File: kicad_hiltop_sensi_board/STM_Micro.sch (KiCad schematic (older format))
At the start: 19 parts, among them SW1 SW_Push, U22 STM32F072RBTx, Y2 8MHZ, Y3 ABS25-32.768KHZ-6-T

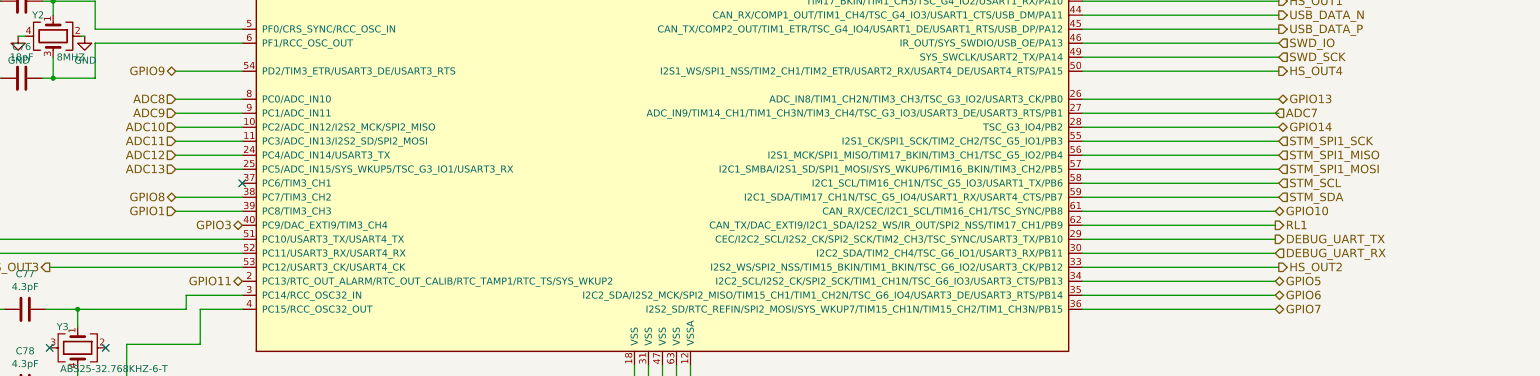
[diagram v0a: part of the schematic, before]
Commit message: Changes to Sensi board after review
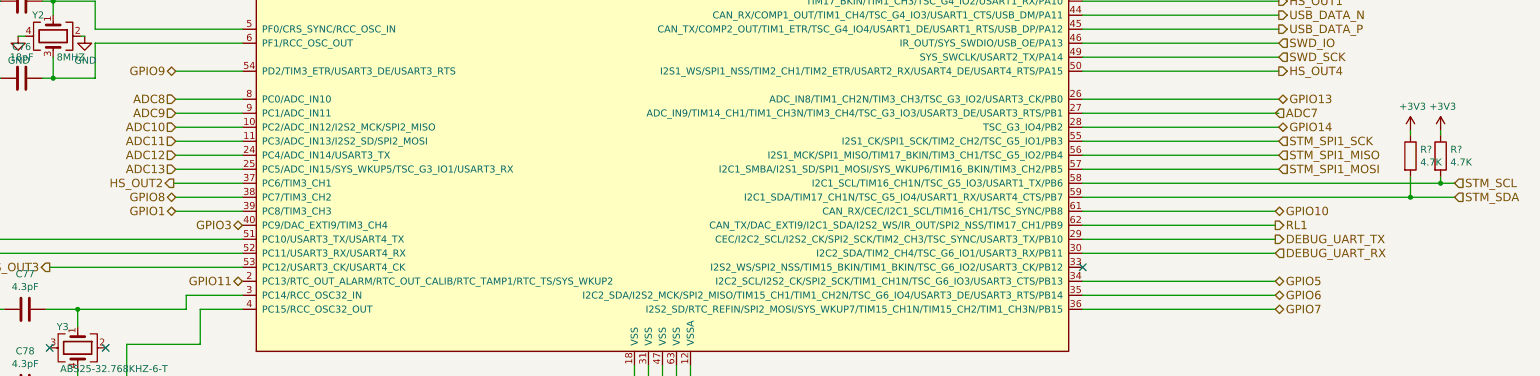
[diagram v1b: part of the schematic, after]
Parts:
- added R? (x2): 4.7K, symbol device:R
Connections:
- net +3V3: now also R?.1, R?.1
- net HS_OUT2: now also U22.37 (PC6/TIM3_CH1); no longer U22.33 (I2S2_WS/SPI2_NSS/TIM15_BKIN/TIM1_BKIN/TSC_G6_IO2/USART3_CK/PB12)
- net STM_SCL: now also R?.2
- net STM_SDA: now also R?.2
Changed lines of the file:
@@
 	10400 4575 11800 4575
 Wire Wire Line
-	10400 5475 11800 5475
+	10400 5475 12740 5475
 Wire Wire Line
 	10400 5575 11775 5575
@@
 	10400 4975 11800 4975
 Wire Wire Line
-	10400 5375 11800 5375
+	10400 5375 12955 5375
 Wire Wire Line
 	10400 6175 11775 6175
@@
 Text HLabel 2500 5775 0    60   BiDi ~ 0
 DUT1_UART_RX_GPIO15
-Text HLabel 3925 5575 0    60   Input ~ 0
+Text HLabel 3925 5575 0    60   3State ~ 0
 GPIO1
 Wire Wire Line
@@
 Text HLabel 11800 5275 2    60   Input ~ 0
 STM_SPI1_MOSI
-Text HLabel 11800 5375 2    60   Input ~ 0
+Text HLabel 13055 5375 2    60   Input ~ 0
 STM_SCL
-Text HLabel 11800 5475 2    60   Input ~ 0
+Text HLabel 13055 5475 2    60   Input ~ 0
 STM_SDA
-NoConn ~ 4400 5375
 NoConn ~ 4400 3475
 NoConn ~ 3425 6550
@@
 Text HLabel 11800 3075 2    60   Input ~ 0
 ADC1
-Text HLabel 11800 5975 2    60   Output ~ 0
+Text HLabel 3910 5375 0    60   Output ~ 0
 HS_OUT2
 Text HLabel 4400 5675 0    60   BiDi ~ 0
@@
 Wire Wire Line
 	4400 5875 2500 5875
-Wire Wire Line
-	10400 5975 11800 5975
 Text HLabel 3925 4975 0    60   Input ~ 0
 ADC10
@@
 Wire Wire Line
 	3250 4325 3275 4325
+Wire Wire Line
+	4400 5375 3910 5375
+NoConn ~ 10400 5975
+$Comp
+L device:R R?
+U 1 1 63797E89
+P 12955 5180
+F 0 "R?" H 13025 5226 50  0000 L CNN
+F 1 "4.7K" H 13025 5135 50  0000 L CNN
+F 2 "" V 12885 5180 50  0001 C CNN
+F 3 "" H 12955 5180 50  0001 C CNN
+	1    12955 5180
+	1    0    0    -1
+$EndComp
+$Comp
+L device:R R?
+U 1 1 63798365
+P 12740 5180
+F 0 "R?" H 12810 5226 50  0000 L CNN
+F 1 "4.7K" H 12810 5135 50  0000 L CNN
+F 2 "" V 12670 5180 50  0001 C CNN
+F 3 "" H 12740 5180 50  0001 C CNN
+	1    12740 5180
+	1    0    0    -1
+$EndComp
+$Comp
+L power:+3V3 #PWR?
+U 1 1 63798567
+P 12740 5000
+F 0 "#PWR?" H 12740 4850 50  0001 C CNN
+F 1 "+3V3" H 12755 5173 50  0000 C CNN
+F 2 "" H 12740 5000 50  0001 C CNN
+F 3 "" H 12740 5000 50  0001 C CNN
+	1    12740 5000
+	1    0    0    -1
+$EndComp
+$Comp
+L power:+3V3 #PWR?
+U 1 1 6379878A
+P 12955 5000
+F 0 "#PWR?" H 12955 4850 50  0001 C CNN
+F 1 "+3V3" H 12970 5173 50  0000 C CNN
+F 2 "" H 12955 5000 50  0001 C CNN
+F 3 "" H 12955 5000 50  0001 C CNN
+	1    12955 5000
+	1    0    0    -1
+$EndComp
+Wire Wire Line
+	12955 5330 12955 5375
+Connection ~ 12955 5375
+Wire Wire Line
+	12955 5375 13055 5375
+Wire Wire Line
+	12740 5330 12740 5475
+Connection ~ 12740 5475
+Wire Wire Line
+	12740 5475 13055 5475
+Wire Wire Line
+	12740 5030 12740 5000
+Wire Wire Line
+	12955 5030 12955 5000
 $EndSCHEMATC

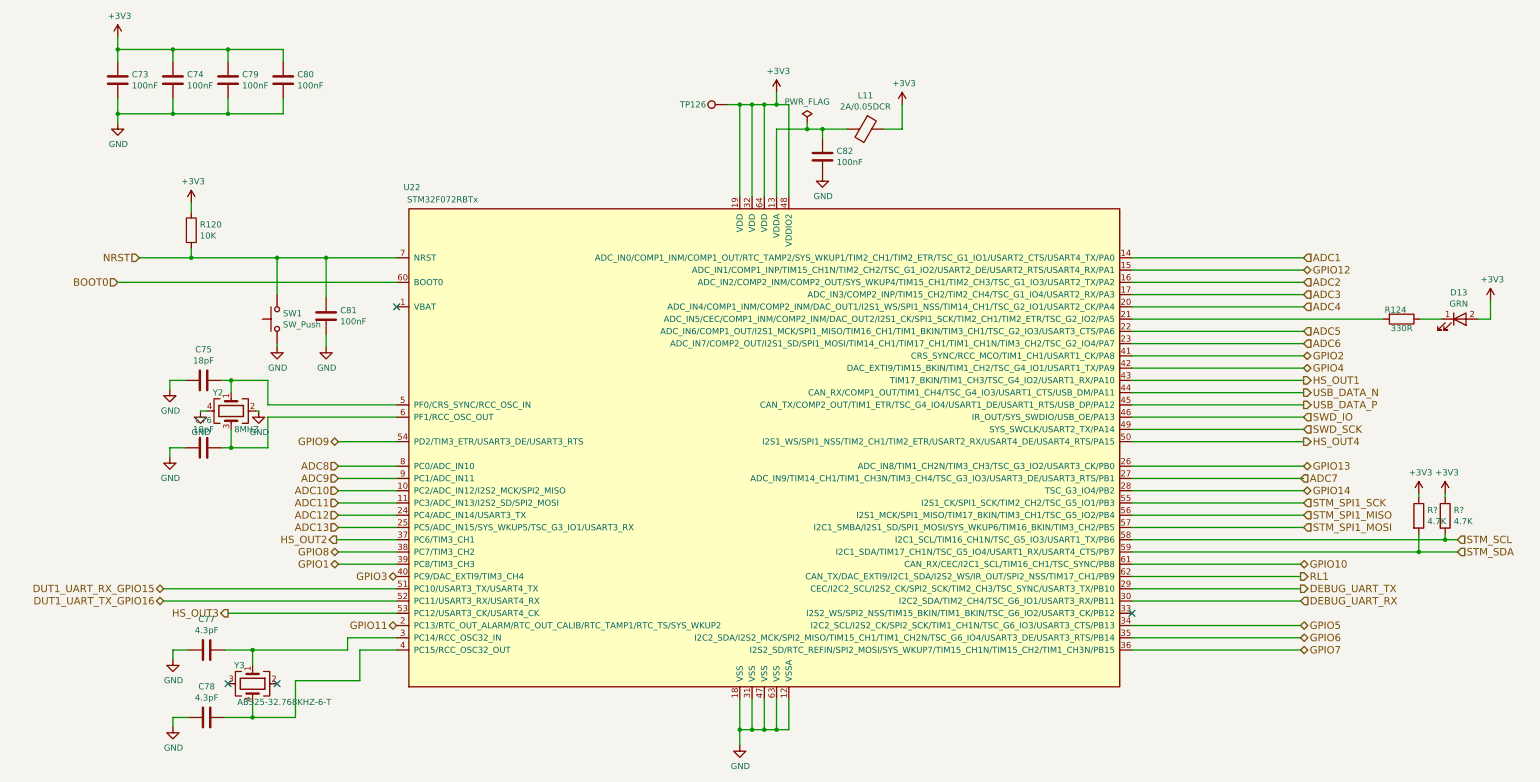
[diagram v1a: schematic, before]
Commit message: Sensi board schematic updated from comments
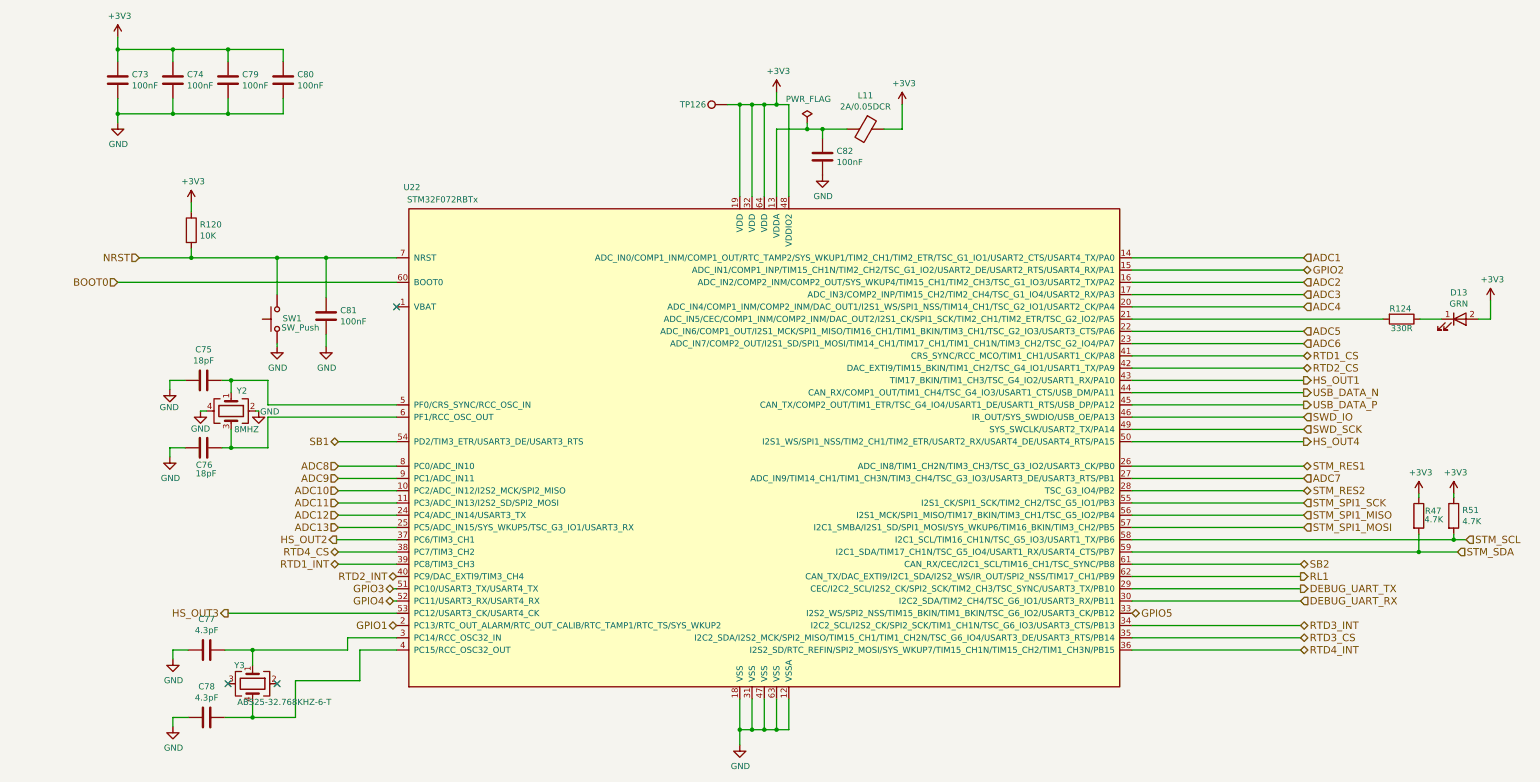
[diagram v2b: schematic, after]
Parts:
- gave numbers to parts that had none: 2
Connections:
- net DUT1_UART_RX_GPIO15 is gone; now on net GPIO3: U22.51 (PC10/USART3_TX/USART4_TX)
- net DUT1_UART_TX_GPIO16 is gone; now on net GPIO4: U22.52 (PC11/USART3_RX/USART4_RX)
- net GPIO11 is gone; now on net GPIO1: U22.2 (PC13/RTC_OUT_ALARM/RTC_OUT_CALIB/RTC_TAMP1/RTC_TS/SYS_WKUP2)
- net GPIO12 is gone; now on net GPIO2: U22.15 (ADC_IN1/COMP1_INP/TIM15_CH1N/TIM2_CH2/TSC_G1_IO2/USART2_DE/USART2_RTS/USART4_RX/PA1)
- net GPIO1: no longer U22.39 (PC8/TIM3_CH3)
- net GPIO2: no longer U22.41 (CRS_SYNC/RCC_MCO/TIM1_CH1/USART1_CK/PA8)
- net GPIO3: no longer U22.40 (PC9/DAC_EXTI9/TIM3_CH4)
- net GPIO4: no longer U22.42 (DAC_EXTI9/TIM15_BKIN/TIM1_CH2/TSC_G4_IO1/USART1_TX/PA9)
- net GPIO5: now also U22.33 (I2S2_WS/SPI2_NSS/TIM15_BKIN/TIM1_BKIN/TSC_G6_IO2/USART3_CK/PB12); no longer U22.34 (I2C2_SCL/I2S2_CK/SPI2_SCK/TIM1_CH1N/TSC_G6_IO3/USART3_CTS/PB13)
- net GPIO10 renamed SB2
- net GPIO13 renamed STM_RES1
- net GPIO14 renamed STM_RES2
- net GPIO6 renamed RTD3_CS
- net GPIO7 renamed RTD4_INT
- net GPIO8 renamed RTD4_CS
- net GPIO9 renamed SB1
- new net RTD1_CS: U22.41 (CRS_SYNC/RCC_MCO/TIM1_CH1/USART1_CK/PA8)
- new net RTD1_INT: U22.39 (PC8/TIM3_CH3)
- new net RTD2_CS: U22.42 (DAC_EXTI9/TIM15_BKIN/TIM1_CH2/TSC_G4_IO1/USART1_TX/PA9)
- new net RTD2_INT: U22.40 (PC9/DAC_EXTI9/TIM3_CH4)
- new net RTD3_INT: U22.34 (I2C2_SCL/I2S2_CK/SPI2_SCK/TIM1_CH1N/TSC_G6_IO3/USART3_CTS/PB13)
- no-connect marks 4 -> 3
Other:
- moved on the sheet: R51
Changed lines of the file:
@@
 $Descr A3 16535 11693
 encoding utf-8
-Sheet 5 11
+Sheet 4 11
 Title ""
 Date "2019-10-01"
@@
 U 1 1 5F9632BE
 P 3425 3575
-F 0 "SW1" V 3471 3527 50  0000 R CNN
-F 1 "SW_Push" V 3380 3527 50  0000 R CNN
+F 0 "SW1" V 3430 3530 50  0000 R CNN
+F 1 "SW_Push" V 3355 3540 50  0000 R CNN
 F 2 "Button_Switch_SMD:SW_SPST_B3U-1000P" H 3425 3775 50  0001 C CNN
 F 3 "" H 3425 3775 50  0001 C CNN
@@
 U 1 1 5F97410A
 P 3050 4325
-F 0 "Y2" V 2900 4175 50  0000 L CNN
+F 0 "Y2" V 2885 4370 50  0000 L CNN
 F 1 "8MHZ" V 3200 4350 50  0000 L CNN
 F 2 "Crystal:Crystal_SMD_Abracon_ABM3C-4Pin_5.0x3.2mm" H 3050 4325 50  0001 C CNN
@@
 P 2550 4150
 F 0 "#PWR0182" H 2550 3900 50  0001 C CNN
-F 1 "GND" H 2555 3977 50  0000 C CNN
+F 1 "GND" H 2545 4005 50  0000 C CNN
 F 2 "" H 2550 4150 50  0001 C CNN
 F 3 "" H 2550 4150 50  0001 C CNN
@@
 U 1 1 5F97DA93
 P 2825 4625
-F 0 "C76" V 2600 4625 50  0000 C CNN
-F 1 "18pF" V 2675 4625 50  0000 C CNN
+F 0 "C76" V 2965 4630 50  0000 C CNN
+F 1 "18pF" V 3035 4645 50  0000 C CNN
 F 2 "Capacitor_SMD:C_0603_1608Metric" H 2863 4475 50  0001 C CNN
 F 3 "" H 2825 4625 50  0001 C CNN
@@
 Wire Wire Line
 	10400 4975 11800 4975
-Wire Wire Line
-	10400 5375 12955 5375
 Wire Wire Line
 	10400 6175 11775 6175
@@
 U 1 1 5CB16726
 P 12600 3575
-F 0 "R124" V 12525 3525 50  0000 C CNN
+F 0 "R124" V 12515 3565 50  0000 C CNN
 F 1 "330R" V 12675 3575 50  0000 C CNN
 F 2 "Resistor_SMD:R_0603_1608Metric" V 12530 3575 50  0001 C CNN
@@
 	13325 3575 13225 3575
 Text HLabel 11800 3975 2    60   BiDi ~ 0
-GPIO4
+RTD2_CS
 Text HLabel 11800 4175 2    60   Output ~ 0
 USB_DATA_N
@@
 USB_DATA_P
 Text HLabel 11800 3875 2    60   BiDi ~ 0
-GPIO2
+RTD1_CS
 Text HLabel 11800 4775 2    60   BiDi ~ 0
-GPIO13
+STM_RES1
 Text HLabel 11775 5575 2    60   BiDi ~ 0
-GPIO10
+SB2
 Text HLabel 11775 6075 2    60   BiDi ~ 0
-GPIO5
+RTD3_INT
 Text HLabel 3925 4575 0    60   BiDi ~ 0
-GPIO9
+SB1
 Text HLabel 4400 6075 0    60   BiDi ~ 0
-GPIO11
+GPIO1
 Text HLabel 11800 4975 2    60   BiDi ~ 0
-GPIO14
+STM_RES2
 Text HLabel 11775 6275 2    60   BiDi ~ 0
-GPIO7
+RTD4_INT
 Text HLabel 3925 5175 0    60   Input ~ 0
 ADC12
@@
 ADC13
 Text HLabel 11800 3175 2    60   BiDi ~ 0
-GPIO12
+GPIO2
 Text HLabel 11775 5675 2    60   Output ~ 0
 RL1
-Text HLabel 2500 5775 0    60   BiDi ~ 0
-DUT1_UART_RX_GPIO15
 Text HLabel 3925 5575 0    60   3State ~ 0
-GPIO1
+RTD1_INT
 Wire Wire Line
 	10400 5075 11800 5075
@@
 Wire Wire Line
 	10400 3175 11800 3175
-Text HLabel 2500 5875 0    60   BiDi ~ 0
-DUT1_UART_TX_GPIO16
 Text HLabel 3925 5475 0    60   BiDi ~ 0
-GPIO8
+RTD4_CS
 Wire Wire Line
 	2125 3275 4400 3275
@@
 Text HLabel 11800 5275 2    60   Input ~ 0
 STM_SPI1_MOSI
-Text HLabel 13055 5375 2    60   Input ~ 0
+Text HLabel 13125 5375 2    60   Input ~ 0
 STM_SCL
 Text HLabel 13055 5475 2    60   Input ~ 0
@@
 HS_OUT2
 Text HLabel 4400 5675 0    60   BiDi ~ 0
-GPIO3
-Text HLabel 11775 6175 2    60   BiDi ~ 0
-GPIO6
+RTD2_INT
 Text HLabel 11775 5875 2    60   Input ~ 0
 DEBUG_UART_RX
 Text HLabel 3025 5975 0    60   Output ~ 0
 HS_OUT3
-Wire Wire Line
-	2500 5775 4400 5775
-Wire Wire Line
-	4400 5875 2500 5875
 Text HLabel 3925 4975 0    60   Input ~ 0
 ADC10
@@
 Text HLabel 11800 3775 2    60   Input ~ 0
 ADC6
-Text HLabel 11775 4875 2    60   Input ~ 0
+Text HLabel 11800 4875 2    60   Input ~ 0
 ADC7
 $Comp
@@
 P 7750 1975
 F 0 "#FLG0102" H 7750 2050 50  0001 C CNN
-F 1 "PWR_FLAG" H 7750 2148 50  0000 C CNN
+F 1 "PWR_FLAG" H 7760 2170 50  0000 C CNN
 F 2 "" H 7750 1975 50  0001 C CNN
 F 3 "" H 7750 1975 50  0001 C CNN
@@
 P 3275 4325
 F 0 "#PWR0162" H 3275 4075 50  0001 C CNN
-F 1 "GND" H 3280 4152 50  0000 C CNN
+F 1 "GND" H 3365 4320 50  0000 C CNN
 F 2 "" H 3275 4325 50  0001 C CNN
 F 3 "" H 3275 4325 50  0001 C CNN
@@
 P 2800 4325
 F 0 "#PWR0165" H 2800 4075 50  0001 C CNN
-F 1 "GND" H 2805 4152 50  0000 C CNN
+F 1 "GND" H 2800 4180 50  0000 C CNN
 F 2 "" H 2800 4325 50  0001 C CNN
 F 3 "" H 2800 4325 50  0001 C CNN
@@
 Wire Wire Line
 	4400 5375 3910 5375
-NoConn ~ 10400 5975
-$Comp
-L device:R R?
+$Comp
+L device:R R51
 U 1 1 63797E89
-P 12955 5180
-F 0 "R?" H 13025 5226 50  0000 L CNN
-F 1 "4.7K" H 13025 5135 50  0000 L CNN
-F 2 "" V 12885 5180 50  0001 C CNN
-F 3 "" H 12955 5180 50  0001 C CNN
-	1    12955 5180
-	1    0    0    -1
-$EndComp
-$Comp
-L device:R R?
+P 13025 5180
+F 0 "R51" H 13095 5226 50  0000 L CNN
+F 1 "4.7K" H 13095 5135 50  0000 L CNN
+F 2 "" V 12955 5180 50  0001 C CNN
+F 3 "" H 13025 5180 50  0001 C CNN
+	1    13025 5180
+	1    0    0    -1
+$EndComp
+$Comp
+L device:R R47
 U 1 1 63798365
 P 12740 5180
-F 0 "R?" H 12810 5226 50  0000 L CNN
-F 1 "4.7K" H 12810 5135 50  0000 L CNN
+F 0 "R47" H 12790 5220 50  0000 L CNN
+F 1 "4.7K" H 12785 5150 50  0000 L CNN
 F 2 "" V 12670 5180 50  0001 C CNN
 F 3 "" H 12740 5180 50  0001 C CNN
@@
 $EndComp
 $Comp
-L power:+3V3 #PWR?
+L power:+3V3 #PWR0127
 U 1 1 63798567
 P 12740 5000
-F 0 "#PWR?" H 12740 4850 50  0001 C CNN
+F 0 "#PWR0127" H 12740 4850 50  0001 C CNN
 F 1 "+3V3" H 12755 5173 50  0000 C CNN
 F 2 "" H 12740 5000 50  0001 C CNN
@@
 $EndComp
 $Comp
-L power:+3V3 #PWR?
+L power:+3V3 #PWR0153
 U 1 1 6379878A
-P 12955 5000
-F 0 "#PWR?" H 12955 4850 50  0001 C CNN
-F 1 "+3V3" H 12970 5173 50  0000 C CNN
-F 2 "" H 12955 5000 50  0001 C CNN
-F 3 "" H 12955 5000 50  0001 C CNN
-	1    12955 5000
-	1    0    0    -1
-$EndComp
-Wire Wire Line
-	12955 5330 12955 5375
-Connection ~ 12955 5375
-Wire Wire Line
-	12955 5375 13055 5375
+P 13025 5000
+F 0 "#PWR0153" H 13025 4850 50  0001 C CNN
+F 1 "+3V3" H 13040 5173 50  0000 C CNN
+F 2 "" H 13025 5000 50  0001 C CNN
+F 3 "" H 13025 5000 50  0001 C CNN
+	1    13025 5000
+	1    0    0    -1
+$EndComp
+Wire Wire Line
+	13025 5330 13025 5375
+Connection ~ 13025 5375
+Wire Wire Line
+	13025 5375 13125 5375
 Wire Wire Line
 	12740 5330 12740 5475
@@
 	12740 5030 12740 5000
 Wire Wire Line
-	12955 5030 12955 5000
+	13025 5030 13025 5000
+Text HLabel 4375 5775 0    60   BiDi ~ 0
+GPIO3
+Text HLabel 4375 5875 0    60   BiDi ~ 0
+GPIO4
+Text HLabel 11775 6175 2    60   BiDi ~ 0
+RTD3_CS
+Text HLabel 10400 5975 2    60   BiDi ~ 0
+GPIO5
+Wire Wire Line
+	10400 5375 13025 5375
+Wire Wire Line
+	4375 5775 4400 5775
+Wire Wire Line
+	4375 5875 4400 5875
 $EndSCHEMATC

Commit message: Updated sensi board layout
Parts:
- R47, R51: footprint (none) -> Resistor_SMD:R_0603_1608Metric
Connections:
- net GPIO1: now also U22.50 (I2S1_WS/SPI1_NSS/TIM2_CH1/TIM2_ETR/USART2_RX/USART4_DE/USART4_RTS/PA15); no longer U22.2 (PC13/RTC_OUT_ALARM/RTC_OUT_CALIB/RTC_TAMP1/RTC_TS/SYS_WKUP2)
- net GPIO2: now also U22.51 (PC10/USART3_TX/USART4_TX); no longer U22.15 (ADC_IN1/COMP1_INP/TIM15_CH1N/TIM2_CH2/TSC_G1_IO2/USART2_DE/USART2_RTS/USART4_RX/PA1)
- net GPIO3: now also U22.52 (PC11/USART3_RX/USART4_RX); no longer U22.51 (PC10/USART3_TX/USART4_TX)
- net GPIO4: now also U22.53 (PC12/USART3_CK/USART4_CK); no longer U22.52 (PC11/USART3_RX/USART4_RX)
- net HS_OUT3: now also U22.54 (PD2/TIM3_ETR/USART3_DE/USART3_RTS); no longer U22.53 (PC12/USART3_CK/USART4_CK)
- net HS_OUT4: now also U22.61 (CAN_RX/CEC/I2C1_SCL/TIM16_CH1/TSC_SYNC/PB8); no longer U22.50 (I2S1_WS/SPI1_NSS/TIM2_CH1/TIM2_ETR/USART2_RX/USART4_DE/USART4_RTS/PA15)
- net SB1: now also U22.2 (PC13/RTC_OUT_ALARM/RTC_OUT_CALIB/RTC_TAMP1/RTC_TS/SYS_WKUP2); no longer U22.54 (PD2/TIM3_ETR/USART3_DE/USART3_RTS)
- net SB2: now also U22.15 (ADC_IN1/COMP1_INP/TIM15_CH1N/TIM2_CH2/TSC_G1_IO2/USART2_DE/USART2_RTS/USART4_RX/PA1); no longer U22.61 (CAN_RX/CEC/I2C1_SCL/TIM16_CH1/TSC_SYNC/PB8)
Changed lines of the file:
@@
 $Descr A3 16535 11693
 encoding utf-8
-Sheet 4 11
+Sheet 11 11
 Title ""
 Date "2019-10-01"
@@
 Text HLabel 11800 4075 2    60   Output ~ 0
 HS_OUT1
-Text HLabel 11800 4575 2    60   Output ~ 0
+Text HLabel 11775 5575 2    60   Output ~ 0
 HS_OUT4
 Text HLabel 11775 5775 2    60   Output ~ 0
@@
 Text HLabel 11800 4775 2    60   BiDi ~ 0
 STM_RES1
-Text HLabel 11775 5575 2    60   BiDi ~ 0
+Text HLabel 11800 3175 2    60   BiDi ~ 0
 SB2
 Text HLabel 11775 6075 2    60   BiDi ~ 0
 RTD3_INT
-Text HLabel 3925 4575 0    60   BiDi ~ 0
+Text HLabel 4400 6075 0    60   BiDi ~ 0
 SB1
-Text HLabel 4400 6075 0    60   BiDi ~ 0
+Text HLabel 11800 4575 2    60   BiDi ~ 0
 GPIO1
 Text HLabel 11800 4975 2    60   BiDi ~ 0
@@
 Text HLabel 3925 5275 0    60   Input ~ 0
 ADC13
-Text HLabel 11800 3175 2    60   BiDi ~ 0
+Text HLabel 4375 5775 0    60   BiDi ~ 0
 GPIO2
 Text HLabel 11775 5675 2    60   Output ~ 0
@@
 Text HLabel 11775 5875 2    60   Input ~ 0
 DEBUG_UART_RX
-Text HLabel 3025 5975 0    60   Output ~ 0
+Text HLabel 3925 4575 0    60   Output ~ 0
 HS_OUT3
 Text HLabel 3925 4975 0    60   Input ~ 0
@@
 	7750 2025 7875 2025
 Wire Wire Line
-	3025 5975 4400 5975
+	4375 5975 4400 5975
 $Comp
 L power:GND #PWR0162
@@
 F 0 "R51" H 13095 5226 50  0000 L CNN
 F 1 "4.7K" H 13095 5135 50  0000 L CNN
-F 2 "" V 12955 5180 50  0001 C CNN
+F 2 "Resistor_SMD:R_0603_1608Metric" V 12955 5180 50  0001 C CNN
 F 3 "" H 13025 5180 50  0001 C CNN
 	1    13025 5180
@@
 F 0 "R47" H 12790 5220 50  0000 L CNN
 F 1 "4.7K" H 12785 5150 50  0000 L CNN
-F 2 "" V 12670 5180 50  0001 C CNN
+F 2 "Resistor_SMD:R_0603_1608Metric" V 12670 5180 50  0001 C CNN
 F 3 "" H 12740 5180 50  0001 C CNN
 	1    12740 5180
@@
 Wire Wire Line
 	13025 5030 13025 5000
-Text HLabel 4375 5775 0    60   BiDi ~ 0
+Text HLabel 4375 5875 0    60   BiDi ~ 0
 GPIO3
-Text HLabel 4375 5875 0    60   BiDi ~ 0
+Text HLabel 4375 5975 0    60   BiDi ~ 0
 GPIO4
 Text HLabel 11775 6175 2    60   BiDi ~ 0

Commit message: Sensi Board Complete
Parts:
- R47, R51: Devtank (none) -> 101-009
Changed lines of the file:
@@
 F 2 "Resistor_SMD:R_0603_1608Metric" V 12955 5180 50  0001 C CNN
 F 3 "" H 13025 5180 50  0001 C CNN
+F 4 "101-009" H 13025 5180 50  0001 C CNN "Devtank"
 	1    13025 5180
 	1    0    0    -1
@@
 F 2 "Resistor_SMD:R_0603_1608Metric" V 12670 5180 50  0001 C CNN
 F 3 "" H 12740 5180 50  0001 C CNN
+F 4 "101-009" H 12740 5180 50  0001 C CNN "Devtank"
 	1    12740 5180
 	1    0    0    -1
